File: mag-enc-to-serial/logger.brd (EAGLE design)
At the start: 60.6 x 26.7 mm, 28 parts, among them IC1 75176AD, IC2 REG1117, U1 MSP430G2352IPW14

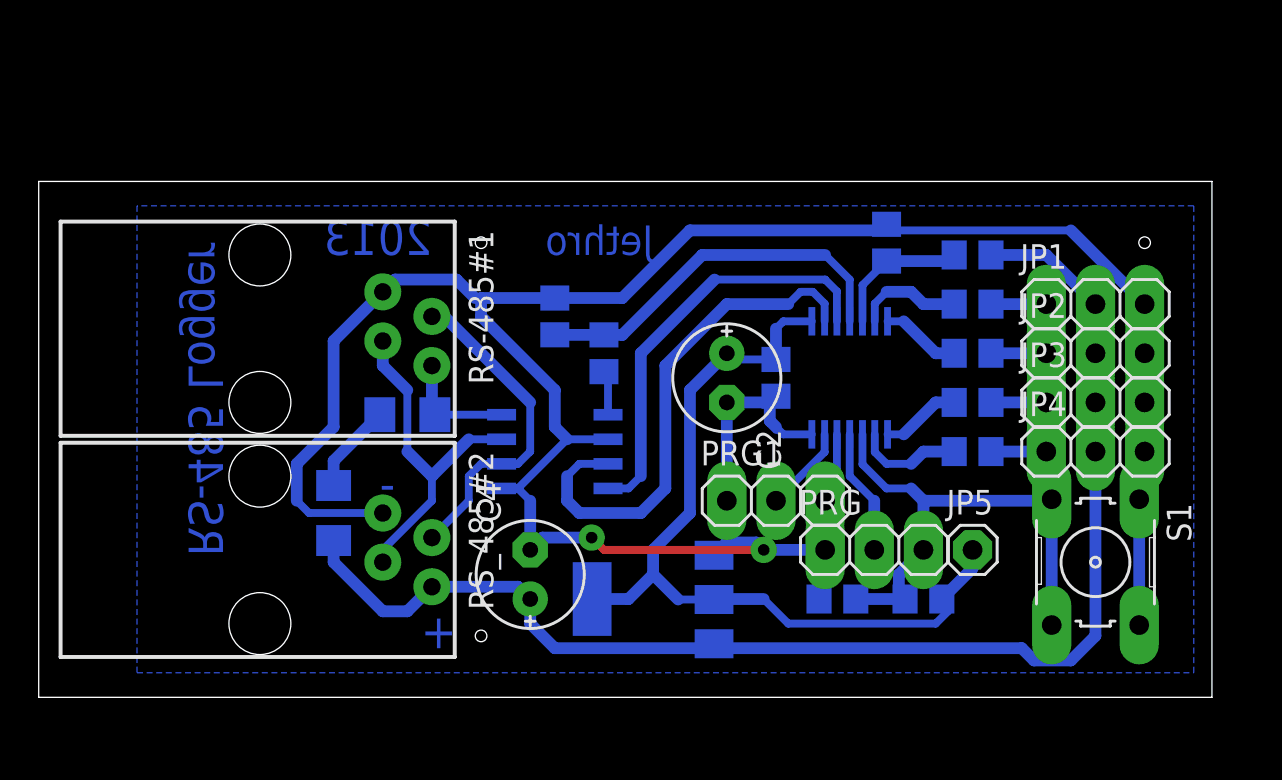
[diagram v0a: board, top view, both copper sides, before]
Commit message: Magnetic encode with MSP430 board
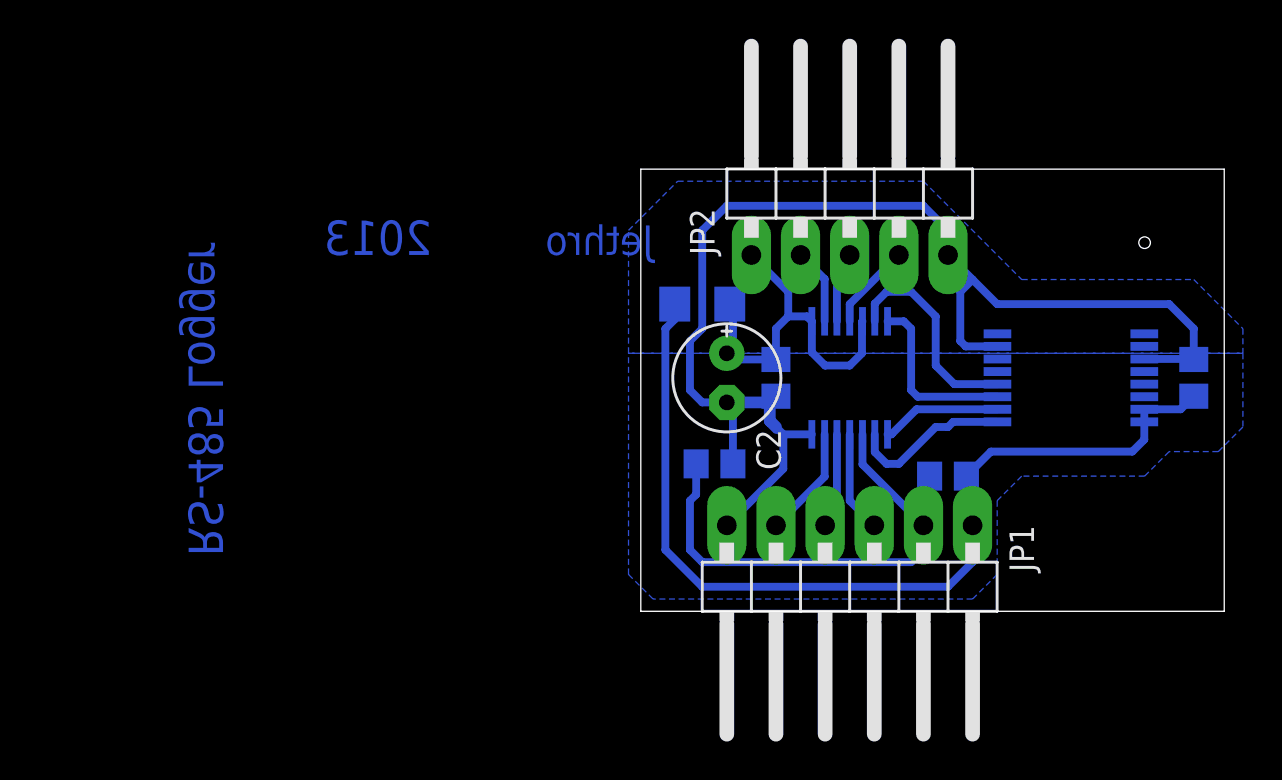
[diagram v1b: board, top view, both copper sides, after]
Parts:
- removed IC2: REG1117, burr-brown:SOT223
- removed JP3, JP4, PRG, PRG1: (no value), pinhead:1X03
- removed JP5: (no value), pinhead:1X01
- removed R10, R9: (no value), rcl:R1206
- removed R11, R12, R2, R3, R4, R5, R6: (no value), rcl:R0805
- removed RS-485#1, RS_485#2: 14867, con-4ucon:14867
- removed S1: (no value), switch-omron:B3F-10XX
- C4: device rcl:E2,5-6E -> rcl:C0805
- IC1: value 75176AD -> AS5040; device 751xx:D_R-PDSO-G8 -> austriamicrosystems:SSOP16
- JP1: device pinhead:1X03 -> pinhead:1X06/90
- JP2: device pinhead:1X03 -> pinhead:1X05/90
- R1: device rcl:R0805 -> rcl:R1206
- moved C4 35.8 mm to (86.4, 64.8), flipped to the bottom, turned to 270 degrees
- moved IC1 26.9 mm to (80.0, 64.8), turned to 90 degrees
- moved JP1 19.8 mm to (68.6, 53.3), turned to 180 degrees
- moved JP2 15.5 mm to (68.6, 74.9)
- moved R1 14.0 mm to (61.0, 68.6), turned to 0 degrees
- moved C3 9.44 mm to (61.6, 60.3), turned to 0 degrees
- moved R8 6.48 mm to (73.7, 59.7)
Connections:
- removed net +5V: C4.+, IC2.3, JP1.2, JP2.2, JP3.2, JP4.2, R10.2, R5.2, RS_485#2.4
- removed net N$12: PRG1.2, U1.13
- removed net N$14: IC1.3, U1.2
- removed net N$16: PRG.2, U1.11
- removed net N$18: PRG1.3, U1.12
- removed net N$19: R10.1, R9.2
- removed net N$20: IC1.8, R9.1, RS-485#1.4
- removed net N$21: IC1.1, R12.1
- removed net N$22: R11.1, R12.2, U1.4
- removed net N$8: JP1.1, R1.2
- removed net N$9: R3.1, U1.8
- new net N$17: JP2.4, U1.4
- net +3V3: now also JP2.1, R1.1, U1.5; no longer IC2.2, IC2.4, JP5.1, R8.1
- net GND: now also C4.1, IC1.11, IC1.7, JP1.6, JP2.5; no longer C4.-, IC1.2, IC1.5, IC2.1, JP1.3, JP2.3, JP3.3, JP4.3, PRG.1, PRG1.1, R11.2, R6.1, RS-485#1.1, RS_485#2.1, S1.1, S1.2
- net N$1: now also JP1.3, U1.11; no longer IC1.6, RS-485#1.2, RS_485#2.2
- net N$10: now also IC1.2, U1.8; no longer R2.1, U1.7
- net N$11: now also IC1.1, U1.9; no longer R1.1, U1.6
- net N$13: now also JP2.2, U1.2; no longer IC1.4, U1.3
- net N$15: now also JP1.2; no longer PRG.3, S1.3, S1.4
- net N$2: now also JP2.3, U1.3; no longer IC1.7, RS-485#1.3, RS_485#2.3
- net N$3: now also JP1.4, U1.12; no longer R5.1, R6.2, U1.5
- net N$4: now also IC1.4, U1.6; no longer R4.1, U1.9
- net N$5: now also IC1.3, U1.7; no longer JP4.1, R4.2
- net N$6: now also C4.2, IC1.15, IC1.16, JP1.1, R1.2, R8.1; no longer JP3.1, R3.2
- net N$7: now also JP1.5, U1.13; no longer JP2.1, R2.2
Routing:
- net +5V: track 76.3 -> 0.00 mm
- net GND: track 131.4 -> 65.1 mm, vias 2 -> 0
- net N$6: track 2.86 -> 49.4 mm
- net N$14: track 26.8 -> 0.00 mm
- net +3V3: track 43.5 -> 19.8 mm
- net N$22: track 19.6 -> 0.00 mm
- net N$13: track 21.8 -> 3.94 mm
- net N$2: track 17.9 -> 3.70 mm
- net N$1: track 17.1 -> 5.23 mm
- net N$16: track 6.50 -> 0.00 mm
- net N$5: track 2.86 -> 9.15 mm
- net N$20: track 6.05 -> 0.00 mm
- net N$4: track 5.53 -> 11.0 mm
- net N$19: track 4.65 -> 0.00 mm
- net N$17: track 0.00 -> 4.48 mm
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- added copper zone on layer 16, net N$6
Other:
- board size 60.6 x 26.7 mm -> 30.2 x 22.9 mm
- board text removed: "+"
- board text removed: "-"
